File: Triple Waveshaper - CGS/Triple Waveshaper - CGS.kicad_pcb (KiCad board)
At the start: 2 copper layers, 74.7 x 61.2 mm, 78 parts, among them J1 CV_1_A, J10 Sum_In_C, J11 IN_C, J12 DC_OUT_A, J13 AC_OUT_A, J14 DC_OUT_B, J15 AC_OUT_B, J16 DC_OUT_C, J17 AC_OUT_C, J18 +12V_Conn, J19 GND_Conn, J2 CV_1_B, J20 -12V_Conn, J21 AUX_In_A, J3 CV_1_C, J4 CV_2_A, J5 CV_2_B, J6 CV_2_C, J7 IN_A, J8 Sum_In_B, J9 IN_B, U1 LM3900

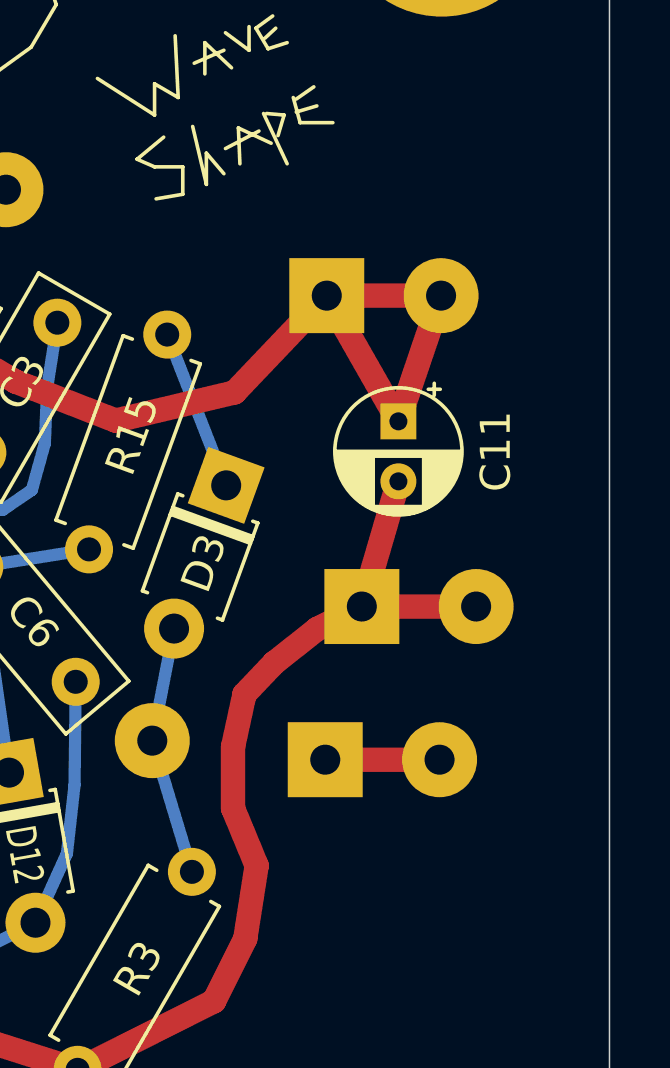
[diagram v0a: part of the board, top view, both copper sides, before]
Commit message: pwr connector silkscreen
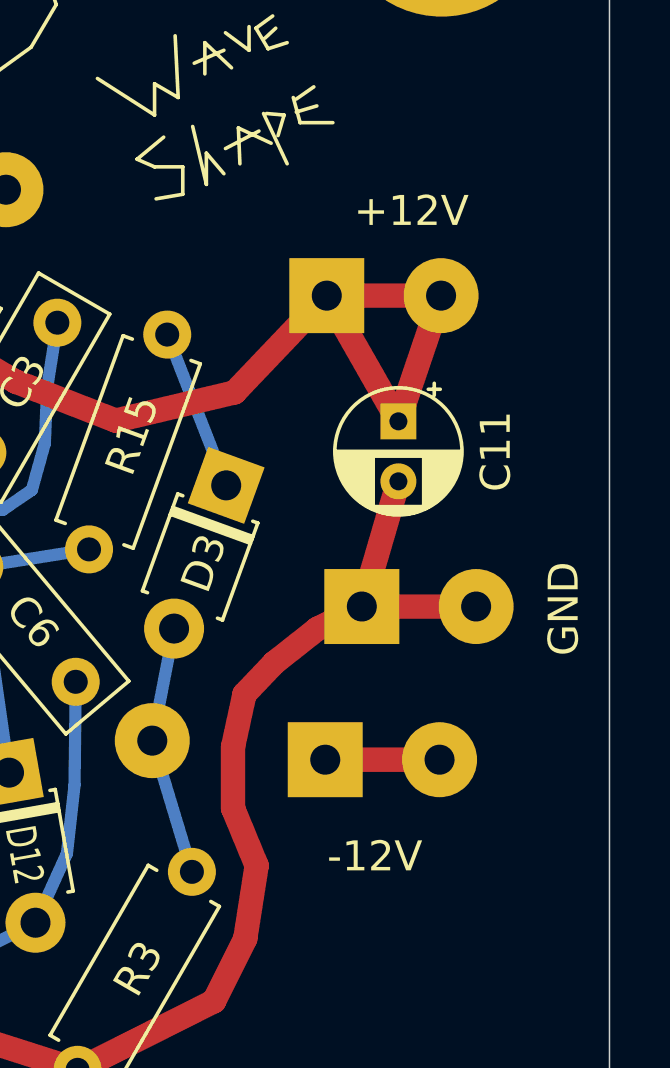
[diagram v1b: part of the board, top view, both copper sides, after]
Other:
- board text added: "+12V"
- board text added: "-12V"
- board text added: "GND"
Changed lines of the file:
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@@
   (general
     (thickness 1.6)
-    (drawings 46)
+    (drawings 49)
     (tracks 267)
     (zones 0)
@@
   )
   (setup
-    (last_trace_width 0.8128)
+    (last_trace_width 0.25)
     (user_trace_width 0.4064)
     (user_trace_width 0.8128)
@@
     )
   )
+  (gr_text GND (at 85.344 41.021 90) (layer F.SilkS)
+    (effects (font (size 1 1) (thickness 0.15)))
+  )
+  (gr_text -12V (at 79.0448 49.276) (layer F.SilkS)
+    (effects (font (size 1 1) (thickness 0.15)))
+  )
+  (gr_text +12V (at 80.264 27.7622) (layer F.SilkS)
+    (effects (font (size 1 1) (thickness 0.15)))
+  )
   (gr_line (start 76.4286 24.0284) (end 77.0128 23.622) (layer F.SilkS) (width 0.12))

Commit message: made silkscreens pretty
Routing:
- added copper zone on B.Cu, net Earth
- added copper zone on F.Cu, net Earth
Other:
- board text added: "LM3900"
